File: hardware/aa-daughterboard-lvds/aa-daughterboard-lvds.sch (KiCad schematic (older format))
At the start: 172 parts, among them CN1 Barrel_Jack, CN10 6P6C, CN11 6P6C, CN12 6P6C, CN13 6P6C, CN14 Conn_01x08, CN15 Conn_01x08, CN16 Conn_01x08, CN17 8P8C, CN18 8P8C, CN19 8P8C, CN2 Conn_01x02, CN20 Conn_01x02, CN21 Conn_01x02, CN22 Conn_01x02, CN23 Conn_01x02, CN24 Conn_01x02, CN25 Conn_01x02, CN3 Conn_01x06, CN4 Conn_01x06, CN5 6P6C, CN6 Conn_01x04, CN7 Conn_01x04, CN8 Conn_01x04, CN9 Conn_01x04, Q1 TN1610H, U1 24LC08, U2 NIS5132xx, U3 uA7805, U4 75ALS192, U5 75ALS192, U6 75ALS192, U7 75ALS192, U8 75ALS192

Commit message: Update to use a shared schematic component/footprint library
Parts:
- A1: footprint aa-daughterboard-lvds:STM32F407_Discovery_P1_P2_Socket -> aa-shared:STM32F407_Discovery_P1_P2_Socket; symbol aa-daughterboard-lvds:STM32F407_Discovery_P1_P2 -> aa-shared:STM32F407_Discovery_P1_P2
- CN10, CN11, CN12, CN13, CN5: footprint aa-daughterboard-lvds:6P6C_Assmann_A-2014-1-4 -> aa-shared:6P6C_Assmann_A-2014-1-4
- CN17, CN18, CN19: footprint aa-daughterboard-lvds:8P8C_Assmann_A-2014-2S-4 -> aa-shared:8P8C_Assmann_A-2014-2S-4
- D10, D11, D12, D13, D14, D15, D16, D17, D18, D19, D6: symbol aa-daughterboard-lvds:D5V0P4UR6SO -> aa-shared:D5V0P4UR6SO
- D23, D24: footprint aa-daughterboard-lvds:D_SOD-128 -> aa-shared:D_SOD-128
- D3: footprint aa-daughterboard-lvds:D_SOD-923 -> aa-shared:D_SOD-923
- F1: footprint aa-daughterboard-lvds:Fuseholder_Clip_5x20_Bel_FC-211-22 -> aa-shared:Fuseholder_Clip_5x20_Bel_FC-211-22
- U2: symbol aa-daughterboard-lvds:NIS5132xx -> aa-shared:NIS5132xx
- U4, U5, U6, U7, U8: symbol aa-daughterboard-lvds:75ALS192 -> aa-shared:75ALS192
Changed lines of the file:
@@
 	4250 5750 4050 5750
 $Comp
-L aa-daughterboard-lvds:+3V #PWR017
+L aa-shared:+3V #PWR017
 U 1 1 5C8B457A
 P 3350 4900
@@
 F 0 "F1" V 3153 1300 50  0000 C CNN
 F 1 "2A" V 3244 1300 50  0000 C CNN
-F 2 "aa-daughterboard-lvds:Fuseholder_Clip_5x20_Bel_FC-211-22" V 3280 1300 50  0001 C CNN
+F 2 "aa-shared:Fuseholder_Clip_5x20_Bel_FC-211-22" V 3280 1300 50  0001 C CNN
 F 3 "~" H 3350 1300 50  0001 C CNN
 	1    3350 1300
@@
 F 0 "D3" V 4254 1629 50  0000 L CNN
 F 1 "DF2S16FS" V 4345 1629 50  0000 L CNN
-F 2 "aa-daughterboard-lvds:D_SOD-923" H 4300 1550 50  0001 C CNN
+F 2 "aa-shared:D_SOD-923" H 4300 1550 50  0001 C CNN
 F 3 "~" H 4300 1550 50  0001 C CNN
 	1    4300 1550
@@
 	3500 14550 3500 14950
 $Comp
-L aa-daughterboard-lvds:+3V #PWR010
+L aa-shared:+3V #PWR010
 U 1 1 62386747
 P 2450 14450
@@
 Connection ~ 2300 1800
 $Comp
-L aa-daughterboard-lvds:NIS5132xx U2
+L aa-shared:NIS5132xx U2
 U 1 1 5CEA4699
 P 4600 3050
@@
 PWM_CAP_A
 $Comp
-L aa-daughterboard-lvds:75ALS192 U5
+L aa-shared:75ALS192 U5
 U 1 1 5EA422B0
 P 7700 10900
@@
 $EndComp
 $Comp
-L aa-daughterboard-lvds:D5V0P4UR6SO D12
+L aa-shared:D5V0P4UR6SO D12
 U 1 1 5EA422B7
 P 10050 10400
@@
 	10400 10400 10650 10400
 $Comp
-L aa-daughterboard-lvds:D5V0P4UR6SO D13
+L aa-shared:D5V0P4UR6SO D13
 U 1 1 5EA422F8
 P 10050 11700
@@
 $EndComp
 $Comp
-L aa-daughterboard-lvds:D5V0P4UR6SO D6
+L aa-shared:D5V0P4UR6SO D6
 U 1 1 5EADDF25
 P 3000 14550
@@
 	10650 9750 10650 10400
 $Comp
-L aa-daughterboard-lvds:75ALS192 U7
+L aa-shared:75ALS192 U7
 U 1 1 5F21D0AA
 P 15700 8250
@@
 $EndComp
 $Comp
-L aa-daughterboard-lvds:75ALS192 U4
+L aa-shared:75ALS192 U4
 U 1 1 5FA1B98E
 P 7700 6750
@@
 $EndComp
 $Comp
-L aa-daughterboard-lvds:D5V0P4UR6SO D10
+L aa-shared:D5V0P4UR6SO D10
 U 1 1 5FA1B995
 P 10050 6250
@@
 	10400 6250 10650 6250
 $Comp
-L aa-daughterboard-lvds:D5V0P4UR6SO D11
+L aa-shared:D5V0P4UR6SO D11
 U 1 1 5FA1B9D5
 P 10050 7550
@@
 F 0 "CN17" H 20570 4604 50  0000 R CNN
 F 1 "8P8C" H 20570 4695 50  0000 R CNN
-F 2 "aa-daughterboard-lvds:8P8C_Assmann_A-2014-2S-4" V 20900 4625 50  0001 C CNN
+F 2 "aa-shared:8P8C_Assmann_A-2014-2S-4" V 20900 4625 50  0001 C CNN
 F 3 "~" V 20900 4625 50  0001 C CNN
 	1    20900 4600
@@
 $EndComp
 $Comp
-L aa-daughterboard-lvds:75ALS192 U6
+L aa-shared:75ALS192 U6
 U 1 1 6306FCC9
 P 15700 4150
@@
 $EndComp
 $Comp
-L aa-daughterboard-lvds:D5V0P4UR6SO D14
+L aa-shared:D5V0P4UR6SO D14
 U 1 1 6306FCD0
 P 18350 3650
@@
 	18700 3650 18950 3650
 $Comp
-L aa-daughterboard-lvds:D5V0P4UR6SO D15
+L aa-shared:D5V0P4UR6SO D15
 U 1 1 6306FD01
 P 18350 4950
@@
 $EndComp
 $Comp
-L aa-daughterboard-lvds:75ALS192 U8
+L aa-shared:75ALS192 U8
 U 1 1 6323CAE9
 P 15700 12250
@@
 	18950 3000 18950 3650
 $Comp
-L aa-daughterboard-lvds:D5V0P4UR6SO D18
+L aa-shared:D5V0P4UR6SO D18
 U 1 1 647AD220
 P 18350 11750
@@
 	18700 11750 18950 11750
 $Comp
-L aa-daughterboard-lvds:D5V0P4UR6SO D19
+L aa-shared:D5V0P4UR6SO D19
 U 1 1 647AD24B
 P 18350 13050
@@
 $EndComp
 $Comp
-L aa-daughterboard-lvds:D5V0P4UR6SO D16
+L aa-shared:D5V0P4UR6SO D16
 U 1 1 64B88892
 P 18350 7750
@@
 	18700 7750 18950 7750
 $Comp
-L aa-daughterboard-lvds:D5V0P4UR6SO D17
+L aa-shared:D5V0P4UR6SO D17
 U 1 1 64B888BD
 P 18350 9050
@@
 F 0 "CN11" H 11620 7604 50  0000 R CNN
 F 1 "6P6C" H 11620 7695 50  0000 R CNN
-F 2 "aa-daughterboard-lvds:6P6C_Assmann_A-2014-1-4" V 11950 7625 50  0001 C CNN
+F 2 "aa-shared:6P6C_Assmann_A-2014-1-4" V 11950 7625 50  0001 C CNN
 F 3 "~" V 11950 7625 50  0001 C CNN
 	1    11950 7600
@@
 F 0 "CN18" H 20570 8704 50  0000 R CNN
 F 1 "8P8C" H 20570 8795 50  0000 R CNN
-F 2 "aa-daughterboard-lvds:8P8C_Assmann_A-2014-2S-4" V 20900 8725 50  0001 C CNN
+F 2 "aa-shared:8P8C_Assmann_A-2014-2S-4" V 20900 8725 50  0001 C CNN
 F 3 "~" V 20900 8725 50  0001 C CNN
 	1    20900 8700
@@
 F 0 "CN19" H 20570 12704 50  0000 R CNN
 F 1 "8P8C" H 20570 12795 50  0000 R CNN
-F 2 "aa-daughterboard-lvds:8P8C_Assmann_A-2014-2S-4" V 20900 12725 50  0001 C CNN
+F 2 "aa-shared:8P8C_Assmann_A-2014-2S-4" V 20900 12725 50  0001 C CNN
 F 3 "~" V 20900 12725 50  0001 C CNN
 	1    20900 12700
@@
 F 0 "CN5" H 4020 14504 50  0000 R CNN
 F 1 "6P6C" H 4020 14595 50  0000 R CNN
-F 2 "aa-daughterboard-lvds:6P6C_Assmann_A-2014-1-4" V 4350 14525 50  0001 C CNN
+F 2 "aa-shared:6P6C_Assmann_A-2014-1-4" V 4350 14525 50  0001 C CNN
 F 3 "~" V 4350 14525 50  0001 C CNN
 	1    4350 14500
@@
 F 0 "CN10" H 11620 5854 50  0000 R CNN
 F 1 "6P6C" H 11620 5945 50  0000 R CNN
-F 2 "aa-daughterboard-lvds:6P6C_Assmann_A-2014-1-4" V 11950 5875 50  0001 C CNN
+F 2 "aa-shared:6P6C_Assmann_A-2014-1-4" V 11950 5875 50  0001 C CNN
 F 3 "~" V 11950 5875 50  0001 C CNN
 	1    11950 5850
@@
 F 0 "CN13" H 11620 11754 50  0000 R CNN
 F 1 "6P6C" H 11620 11845 50  0000 R CNN
-F 2 "aa-daughterboard-lvds:6P6C_Assmann_A-2014-1-4" V 11950 11775 50  0001 C CNN
+F 2 "aa-shared:6P6C_Assmann_A-2014-1-4" V 11950 11775 50  0001 C CNN
 F 3 "~" V 11950 11775 50  0001 C CNN
 	1    11950 11750
@@
 F 0 "CN12" H 11620 10004 50  0000 R CNN
 F 1 "6P6C" H 11620 10095 50  0000 R CNN
-F 2 "aa-daughterboard-lvds:6P6C_Assmann_A-2014-1-4" V 11950 10025 50  0001 C CNN
+F 2 "aa-shared:6P6C_Assmann_A-2014-1-4" V 11950 10025 50  0001 C CNN
 F 3 "~" V 11950 10025 50  0001 C CNN
 	1    11950 10000
@@
 	3550 7650 3500 7650
 $Comp
-L aa-daughterboard-lvds:STM32F407_Discovery_P1_P2 A1
+L aa-shared:STM32F407_Discovery_P1_P2 A1
 U 1 1 5FE84798
 P 2850 6800
 F 0 "A1" H 2850 8275 50  0000 C CNN
 F 1 "STM32F407_Discovery_P1_P2" H 2850 8184 50  0000 C CNN
-F 2 "aa-daughterboard-lvds:STM32F407_Discovery_P1_P2_Socket" H 2850 6850 50  0001 C CNN
+F 2 "aa-shared:STM32F407_Discovery_P1_P2_Socket" H 2850 6850 50  0001 C CNN
 F 3 "~" H 1800 6850 50  0001 C CNN
 	1    2850 6800
@@
 F 0 "D23" H 1950 976 50  0000 C CNN
 F 1 "D_Schottky" H 1950 975 50  0001 C CNN
-F 2 "aa-daughterboard-lvds:D_SOD-128" H 1950 1100 50  0001 C CNN
+F 2 "aa-shared:D_SOD-128" H 1950 1100 50  0001 C CNN
 F 3 "~" H 1950 1100 50  0001 C CNN
 	1    1950 1100
@@
 F 0 "D24" H 1950 1476 50  0000 C CNN
 F 1 "D_Schottky" H 1950 1475 50  0001 C CNN
-F 2 "aa-daughterboard-lvds:D_SOD-128" H 1950 1600 50  0001 C CNN
+F 2 "aa-shared:D_SOD-128" H 1950 1600 50  0001 C CNN
 F 3 "~" H 1950 1600 50  0001 C CNN
 	1    1950 1600

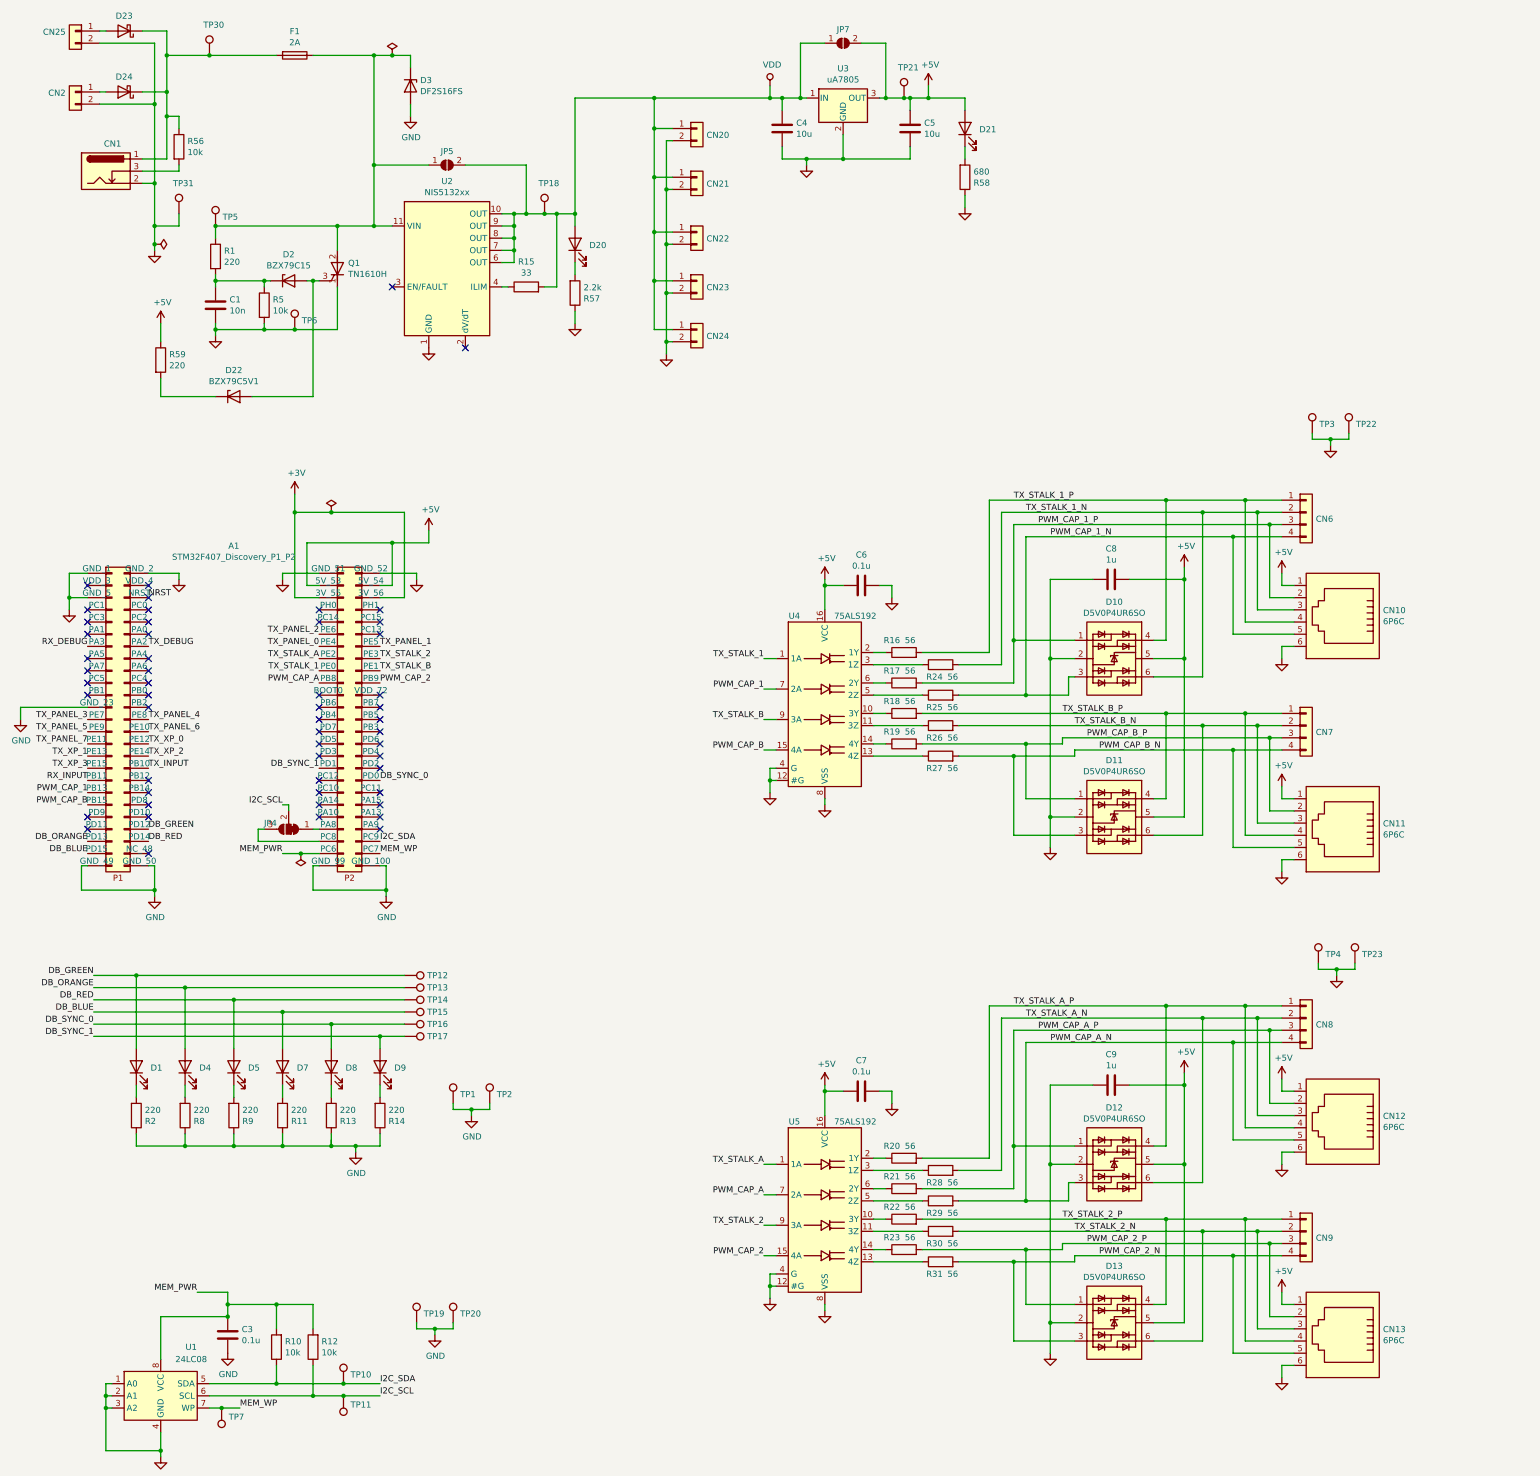
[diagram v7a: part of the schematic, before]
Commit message: Substantial rework of system, new layouts done for daughterboard, power, stalk receiver
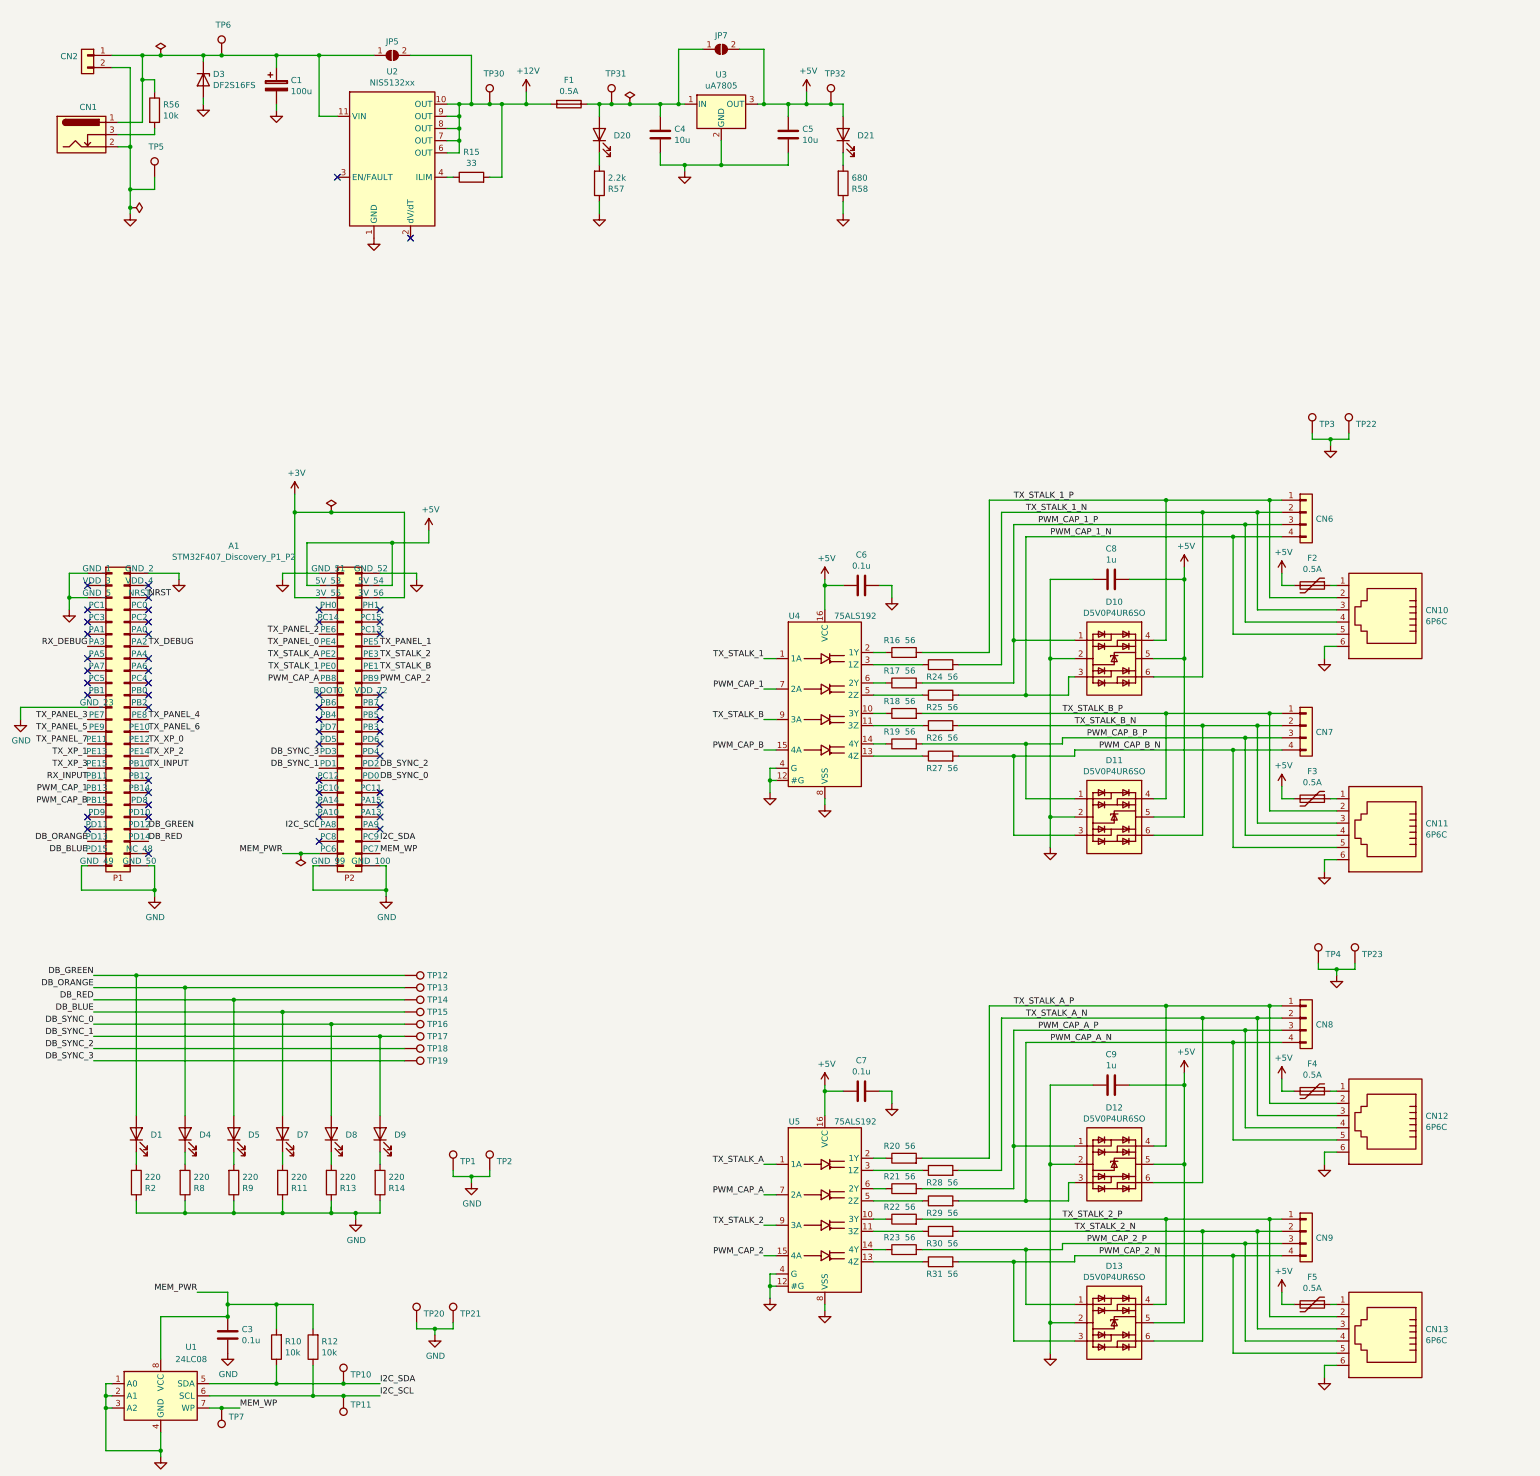
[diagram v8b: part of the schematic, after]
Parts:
- removed C1: 10n, Capacitor_SMD:C_0603_1608Metric, symbol Device:C
- removed CN20, CN21, CN22, CN23, CN24: Conn_01x02, Connector_PinHeader_2.54mm:PinHeader_1x02_P2.54mm_Vertical, symbol Connector_Generic:Conn_01x02
- removed CN25: Conn_01x02, Connector_Wire:SolderWirePad_1x02_P5.08mm_Drill1.5mm, symbol Connector_Generic:Conn_01x02
- removed D2: BZX79C15, Diode_THT:D_DO-35_SOD27_P7.62mm_Horizontal, symbol Device:D_Zener
- removed D22: BZX79C5V1, Diode_THT:D_DO-35_SOD27_P7.62mm_Horizontal, symbol Device:D_Zener
- removed D23, D24: D_Schottky, aa-shared:D_SOD-128, symbol Device:D_Schottky
- removed JP4: SolderJumper_3_Bridged12, Jumper:SolderJumper-3_P1.3mm_Bridged2Bar12_RoundedPad1.0x1.5mm, symbol Jumper:SolderJumper_3_Bridged12
- removed Q1: TN1610H, Package_TO_SOT_THT:TO-220-3_Vertical, symbol Device:Q_SCR_KAG
- removed R1, R59: 220, Resistor_SMD:R_0603_1608Metric, symbol Device:R
- removed R5: 10k, Resistor_SMD:R_0603_1608Metric, symbol Device:R
- removed TP5, TP6: TestPoint, TestPoint:TestPoint_THTPad_D2.0mm_Drill1.0mm, symbol Connector:TestPoint
- added C1: 100u, Capacitor_THT:CP_Radial_D10.0mm_P2.50mm_P5.00mm, symbol Device:CP
- added F2, F3, F4, F5: 0.5A, Fuse:Fuse_0603_1608Metric, symbol Device:Polyfuse
- added TP18, TP19, TP32: TestPoint, TestPoint:TestPoint_THTPad_D2.0mm_Drill1.0mm, symbol Connector:TestPoint
- F1: value 2A -> 0.5A
- renumbered TP19 to TP21, TP18 to TP30, TP21 to TP31, TP31 to TP5, TP30 to TP6
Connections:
- net +5V: now also F2.2, F3.2, F4.2, F5.2, TP32.1; no longer CN10.1, CN11.1, CN12.1, CN13.1, TP31.1
- net GND: now also C1.2
- net I2C_SCL: now also A1.P2_43 (PA8)
- net PWM_CAP_1_P: now also CN10.4; no longer CN10.2
- net PWM_CAP_2_P: now also CN13.4; no longer CN13.2
- net PWM_CAP_A_P: now also CN12.4; no longer CN12.2
- net PWM_CAP_B_P: now also CN11.4; no longer CN11.2
- net TX_STALK_1_P: now also CN10.2; no longer CN10.4
- net TX_STALK_2_P: now also CN13.2; no longer CN13.4
- net TX_STALK_A_P: now also CN12.2; no longer CN12.4
- net TX_STALK_B_P: now also CN11.2; no longer CN11.4
- net at D3.1 (K), JP5.1 (A), U2.11 (VIN): now also CN1.1, CN2.1 (Pin_1), R56.1, TP6.1, C1.1; no longer F1.1
- net DB_SYNC_3: now reaches A1.P2_31 (PD3)
- net DB_SYNC_3: now also TP19.1
- net DB_SYNC_2: now reaches A1.P2_34 (PD2)
- net DB_SYNC_2: now also TP18.1
- net VDD renamed +12V
- net +12V: now also F1.2; no longer C4.1, D20.2 (A), JP7.1 (A), U3.1 (IN)
- new net: C4.1, D20.2 (A), F1.1, JP7.1 (A), TP31.1, U3.1 (IN)
- new net: CN11.1, F3.1
- new net: CN10.1, F2.1
- new net: CN12.1, F4.1
- new net: CN13.1, F5.1
- no-connect marks 59 -> 58
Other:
- moved on the sheet: C4, C5, CN1, CN10, CN11, CN12, CN13, CN2, D1, D20, D21, D3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
